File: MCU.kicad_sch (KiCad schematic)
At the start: 29 parts

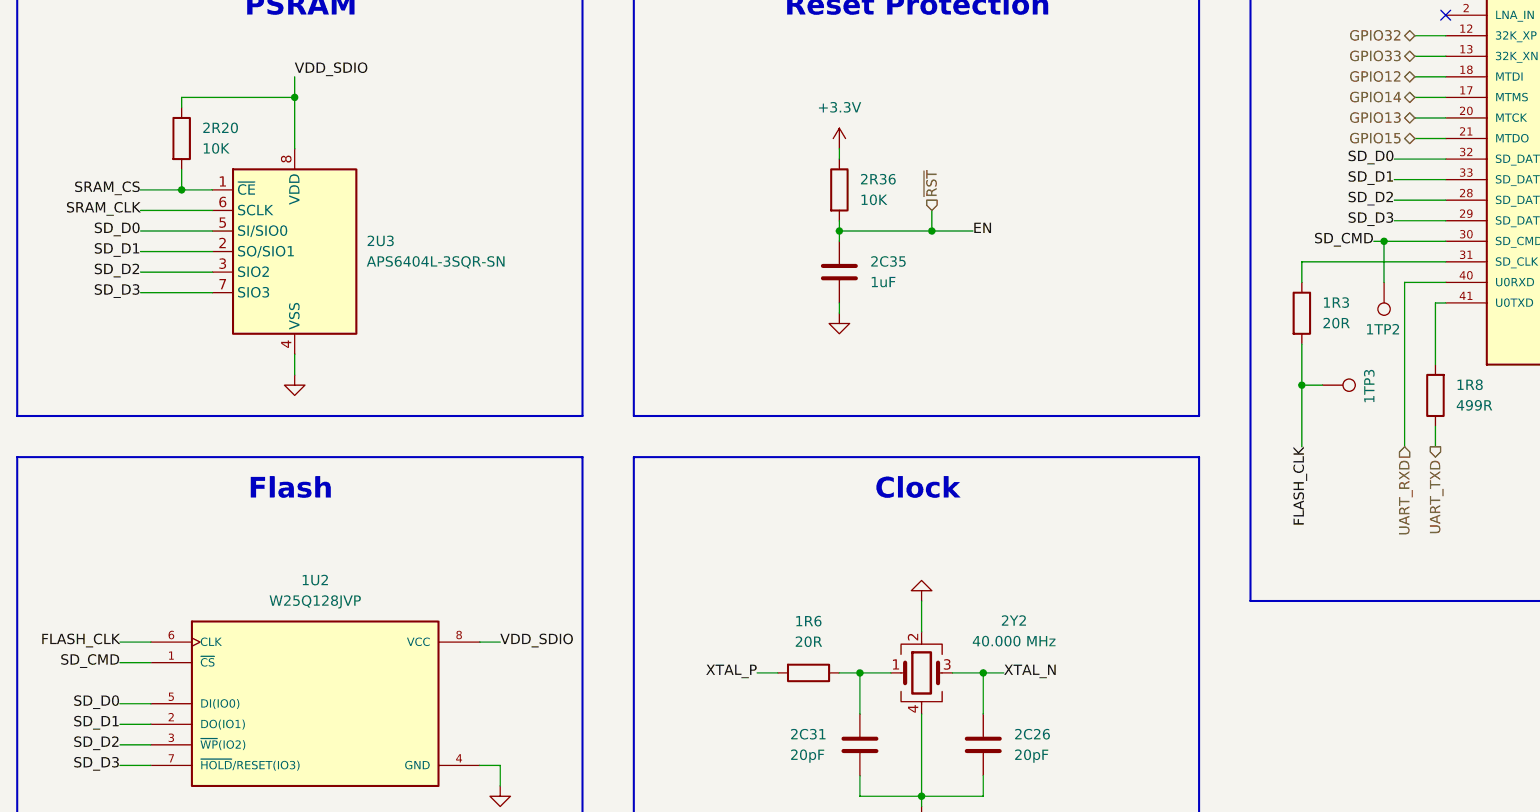
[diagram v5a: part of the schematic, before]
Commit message: fixed Flash and PSRAM to MCU pinout mapping added pull-up to Flash CS pin
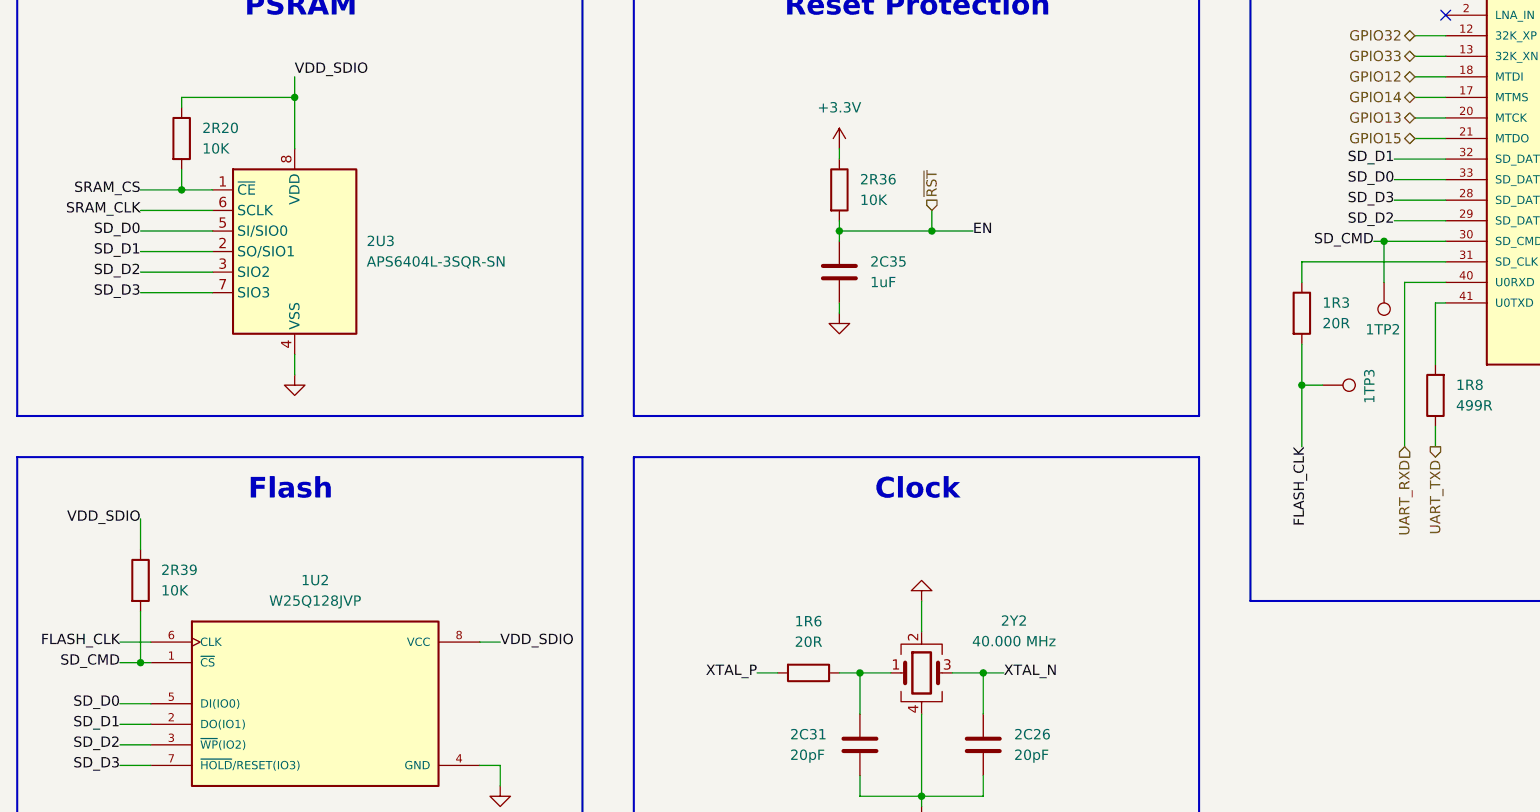
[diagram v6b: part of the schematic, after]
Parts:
- added 2R39: 10K, Resistor_SMD:R_0402_1005Metric, symbol Device:R
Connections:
- net SD_CMD: now also 2R39.2
- net SD_D0: now also 1U4.33 (SD_DATA_1); no longer 1U4.32 (SD_DATA_0)
- net SD_D1: now also 1U4.32 (SD_DATA_0); no longer 1U4.33 (SD_DATA_1)
- net SD_D2: now also 1U4.29 (SD_DATA_3); no longer 1U4.28 (SD_DATA_2)
- net SD_D3: now also 1U4.28 (SD_DATA_2); no longer 1U4.29 (SD_DATA_3)
- net VDD_SDIO: now also 2R39.1
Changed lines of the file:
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@@
 	)
 	(junction
+		(at 31.75 162.56)
+		(diameter 0)
+		(color 0 0 0 0)
+	)
+	(junction
 		(at 135.89 53.34)
 		(diameter 0)
@@
 	(wire
 		(pts
+			(xy 31.75 144.78) (xy 31.75 148.59)
+		)
+		(stroke
+			(width 0)
+			(type default)
+		)
+	)
+	(wire
+		(pts
 			(xy 71.12 63.5) (xy 71.12 66.04)
 		)
@@
 	(wire
 		(pts
+			(xy 31.75 156.21) (xy 31.75 162.56)
+		)
+		(stroke
+			(width 0)
+			(type default)
+		)
+	)
+	(wire
+		(pts
 			(xy 36.83 93.98) (xy 36.83 92.71)
 		)
@@
 	(wire
 		(pts
-			(xy 246.38 44.45) (xy 247.65 44.45)
+			(xy 186.69 105.41) (xy 193.04 105.41)
 		)
 		(stroke
@@
 	(wire
 		(pts
-			(xy 67.31 33.02) (xy 69.85 33.02)
+			(xy 246.38 44.45) (xy 247.65 44.45)
 		)
 		(stroke
@@
 	(wire
 		(pts
-			(xy 243.84 36.83) (xy 247.65 36.83)
+			(xy 67.31 33.02) (xy 69.85 33.02)
 		)
 		(stroke
@@
 	(wire
 		(pts
-			(xy 175.26 128.27) (xy 175.26 135.89)
+			(xy 243.84 36.83) (xy 247.65 36.83)
 		)
 		(stroke
@@
 	(wire
 		(pts
-			(xy 29.21 31.75) (xy 29.21 33.02)
+			(xy 175.26 128.27) (xy 175.26 135.89)
 		)
 		(stroke
@@
 	(wire
 		(pts
-			(xy 29.21 54.61) (xy 29.21 55.88)
+			(xy 29.21 31.75) (xy 29.21 33.02)
 		)
 		(stroke
@@
 	(wire
 		(pts
-			(xy 57.15 66.04) (xy 57.15 67.31)
+			(xy 29.21 54.61) (xy 29.21 55.88)
 		)
 		(stroke
@@
 	(wire
 		(pts
-			(xy 243.84 44.45) (xy 246.38 44.45)
+			(xy 57.15 66.04) (xy 57.15 67.31)
 		)
 		(stroke
@@
 	(wire
 		(pts
-			(xy 186.69 100.33) (xy 193.04 100.33)
+			(xy 243.84 44.45) (xy 246.38 44.45)
 		)
 		(stroke
@@
 	(wire
 		(pts
-			(xy 186.69 107.95) (xy 193.04 107.95)
-		)
-		(stroke
-			(width 0)
-			(type default)
-		)
-	)
-	(wire
-		(pts
 			(xy 73.66 175.26) (xy 76.2 175.26)
 		)
@@
 	(wire
 		(pts
-			(xy 29.21 162.56) (xy 33.02 162.56)
+			(xy 29.21 162.56) (xy 31.75 162.56)
 		)
 		(stroke
@@
 	(wire
 		(pts
+			(xy 186.69 107.95) (xy 193.04 107.95)
+		)
+		(stroke
+			(width 0)
+			(type default)
+		)
+	)
+	(wire
+		(pts
 			(xy 132.08 163.83) (xy 135.89 163.83)
 		)
@@
 	(wire
 		(pts
-			(xy 186.69 105.41) (xy 193.04 105.41)
+			(xy 29.21 66.04) (xy 29.21 67.31)
 		)
 		(stroke
@@
 	(wire
 		(pts
-			(xy 29.21 66.04) (xy 29.21 67.31)
+			(xy 135.89 38.1) (xy 146.05 38.1)
 		)
 		(stroke
@@
 	(wire
 		(pts
-			(xy 135.89 38.1) (xy 146.05 38.1)
+			(xy 186.69 102.87) (xy 193.04 102.87)
 		)
 		(stroke
@@
 	(wire
 		(pts
+			(xy 186.69 100.33) (xy 193.04 100.33)
+		)
+		(stroke
+			(width 0)
+			(type default)
+		)
+	)
+	(wire
+		(pts
 			(xy 135.89 163.83) (xy 135.89 168.91)
 		)
@@
 	(wire
 		(pts
-			(xy 40.64 55.88) (xy 29.21 55.88)
+			(xy 31.75 162.56) (xy 33.02 162.56)
 		)
 		(stroke
@@
 	(wire
 		(pts
-			(xy 189.23 95.25) (xy 193.04 95.25)
+			(xy 40.64 55.88) (xy 29.21 55.88)
 		)
 		(stroke
@@
 	(wire
 		(pts
-			(xy 123.19 38.1) (xy 135.89 38.1)
+			(xy 189.23 95.25) (xy 193.04 95.25)
 		)
 		(stroke
@@
 	(wire
 		(pts
-			(xy 175.26 123.19) (xy 175.26 128.27)
+			(xy 123.19 38.1) (xy 135.89 38.1)
 		)
 		(stroke
@@
 	(wire
 		(pts
-			(xy 129.54 109.22) (xy 134.62 109.22)
+			(xy 175.26 123.19) (xy 175.26 128.27)
 		)
 		(stroke
@@
 	(wire
 		(pts
-			(xy 76.2 175.26) (xy 76.2 177.8)
+			(xy 129.54 109.22) (xy 134.62 109.22)
 		)
 		(stroke
@@
 	(wire
 		(pts
-			(xy 128.27 154.94) (xy 128.27 158.75)
+			(xy 76.2 175.26) (xy 76.2 177.8)
 		)
 		(stroke
@@
 	(wire
 		(pts
-			(xy 54.61 34.29) (xy 54.61 33.02)
+			(xy 128.27 154.94) (xy 128.27 158.75)
 		)
 		(stroke
@@
 	(wire
 		(pts
-			(xy 186.69 102.87) (xy 193.04 102.87)
+			(xy 54.61 34.29) (xy 54.61 33.02)
 		)
 		(stroke
@@
 	)
 	(label "SD_D1"
-		(at 186.69 102.87 180)
+		(at 186.69 100.33 180)
 		(effects
 			(font
@@
 	)
 	(label "SD_D3"
-		(at 186.69 107.95 180)
+		(at 186.69 105.41 180)
 		(effects
 			(font
@@
 	)
 	(label "SD_D0"
-		(at 186.69 100.33 180)
+		(at 186.69 102.87 180)
 		(effects
 			(font
@@
 	)
 	(label "SD_D2"
-		(at 186.69 105.41 180)
+		(at 186.69 107.95 180)
 		(effects
 			(font
@@
 		)
 	)
+	(label "VDD_SDIO"
+		(at 31.75 144.78 180)
+		(effects
+			(font
+				(size 1.27 1.27)
+			)
+			(justify right)
+		)
+	)
 	(label "VDD_SDIO_OUT"
 		(at 247.65 41.91 0)
@@
 					(unit 1)
 				)
+			)
+		)
+	)
+	(symbol
+		(lib_id "Device:R")
+		(at 31.75 152.4 0)
+		(unit 1)
+		(exclude_from_sim no)
+		(in_bom yes)
+		(on_board yes)
+		(dnp no)
+		(fields_autoplaced yes)
+		(property "Reference" "2R39"
+			(at 34.29 151.1299 0)
+			(effects
+				(font
+					(size 1.27 1.27)
+				)
+				(justify left)
+			)
+		)
+		(property "Value" "10K"
+			(at 34.29 153.6699 0)
+			(effects
+				(font
+					(size 1.27 1.27)
+				)
+				(justify left)
+			)
+		)
+		(property "Footprint" "Resistor_SMD:R_0402_1005Metric"
+			(at 29.972 152.4 90)
+			(effects
+				(font
+					(size 1.27 1.27)
+				)
+				(hide yes)
+			)
+		)
+		(property "Datasheet" "~"
+			(at 31.75 152.4 0)
+			(effects
+				(font
+					(size 1.27 1.27)
+				)
+				(hide yes)
+			)
+		)
+		(property "Description" "Resistor"
+			(at 31.75 152.4 0)
+			(effects
+				(font
+					(size 1.27 1.27)
+				)
+				(hide yes)
+			)
+		)
+		(property "MOUSER#" "603-RE0402FRE0710KL"
+			(at 31.75 152.4 0)
+			(effects
+				(font
+					(size 1.27 1.27)
+				)
+				(hide yes)
+			)
+		)
+		(property "IDAnything" "c1vc3q1ecwg38aepd291cy2avj"
+			(at 31.75 152.4 0)
+			(effects
+				(font
+					(size 1.27 1.27)
+				)
+				(hide yes)
+			)
+		)
+		(pin "1"
+		)
+		(pin "2"
+		)
+		(instances
+			(project "Module"
+				(path "/4c939de5-59ef-438d-9f29-5de1016e5f2f/9bdf3d9b-885e-428e-95ba-d4f7bd684dc5"
+					(reference "2R39")
+					(unit 1)
+				)

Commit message: small, cosmetic fixes added project url to front silkscreen
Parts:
- 1TP2, 1TP3, 1TP4: now left out of the parts list
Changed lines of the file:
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@@
 		(unit 1)
 		(exclude_from_sim no)
-		(in_bom yes)
+		(in_bom no)
 		(on_board yes)
 		(dnp no)
@@
 		(unit 1)
 		(exclude_from_sim no)
-		(in_bom yes)
+		(in_bom no)
 		(on_board yes)
 		(dnp no)
@@
 		(unit 1)
 		(exclude_from_sim no)
-		(in_bom yes)
-		(on_board yes)
-		(dnp no)
+		(in_bom no)
+		(on_board yes)
+		(dnp no)

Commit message: added some LCSC part numbers
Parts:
- 1U2: LCSC# (none) -> C190862
- 1U4: LCSC# (none) -> C967021
- 2U3: LCSC# (none) -> C5333729
